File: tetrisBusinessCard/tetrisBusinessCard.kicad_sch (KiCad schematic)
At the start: 498 parts, among them J1 USB_B_Micro, SW1 SW_Push, SW2 SW_Push, SW3 SW_Push, SW4 SW_Push, SW5 SW_Push, SW6 SW_Push, SW7 SW_DPST_x2, SW8 SW_Push, U1 SC091413, U2 W25Q16JVUXIQ, U3 NCP1117-3.3_SOT223, Y1 ABMB-272-T3

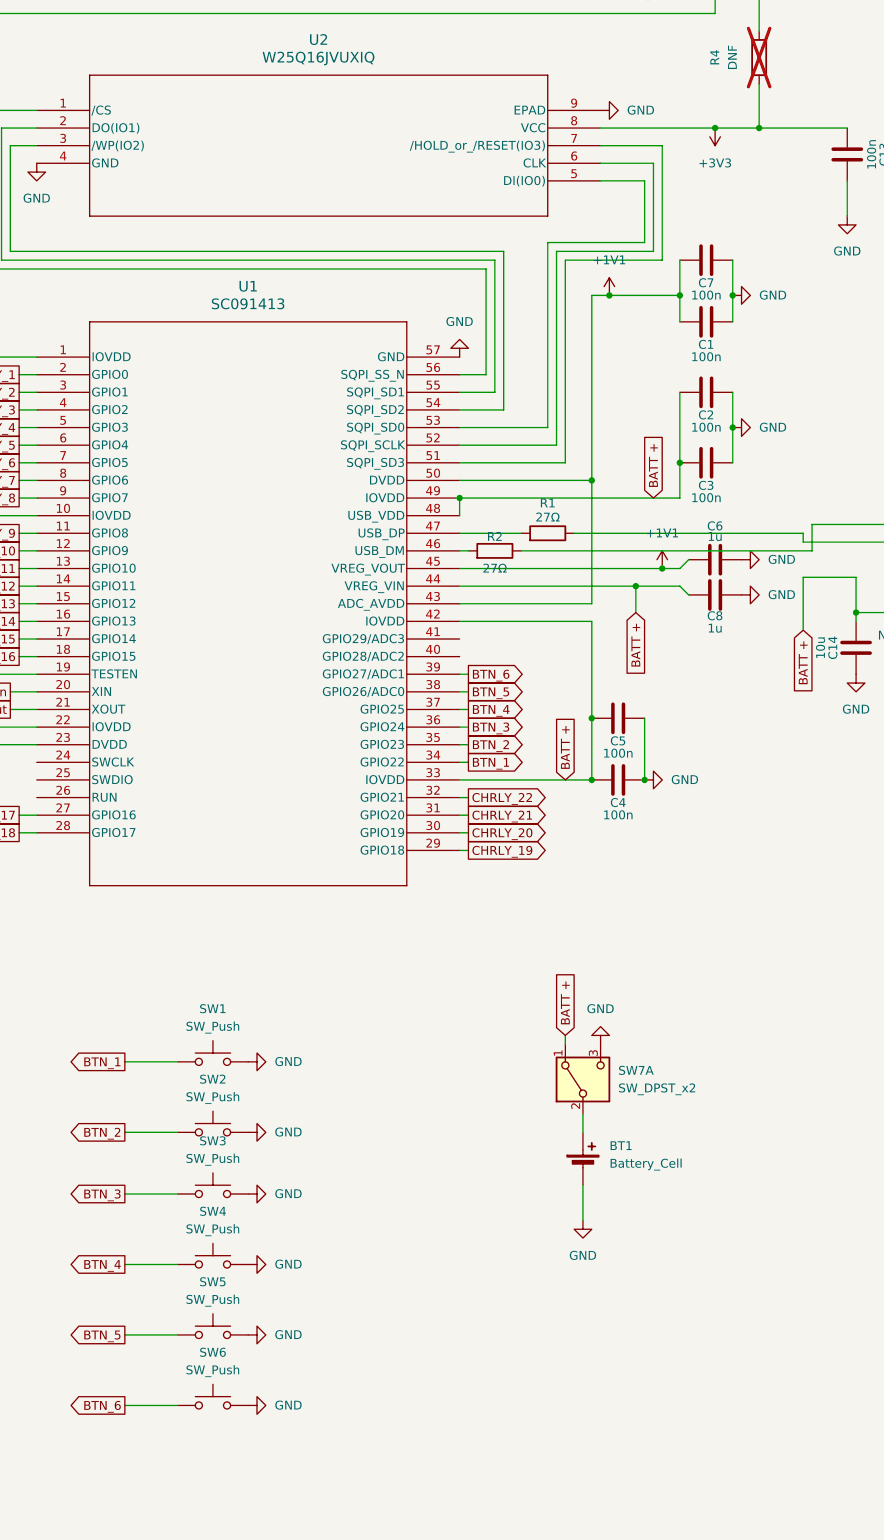
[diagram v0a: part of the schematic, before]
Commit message: Add capacitive touch symbol and update PCB partially
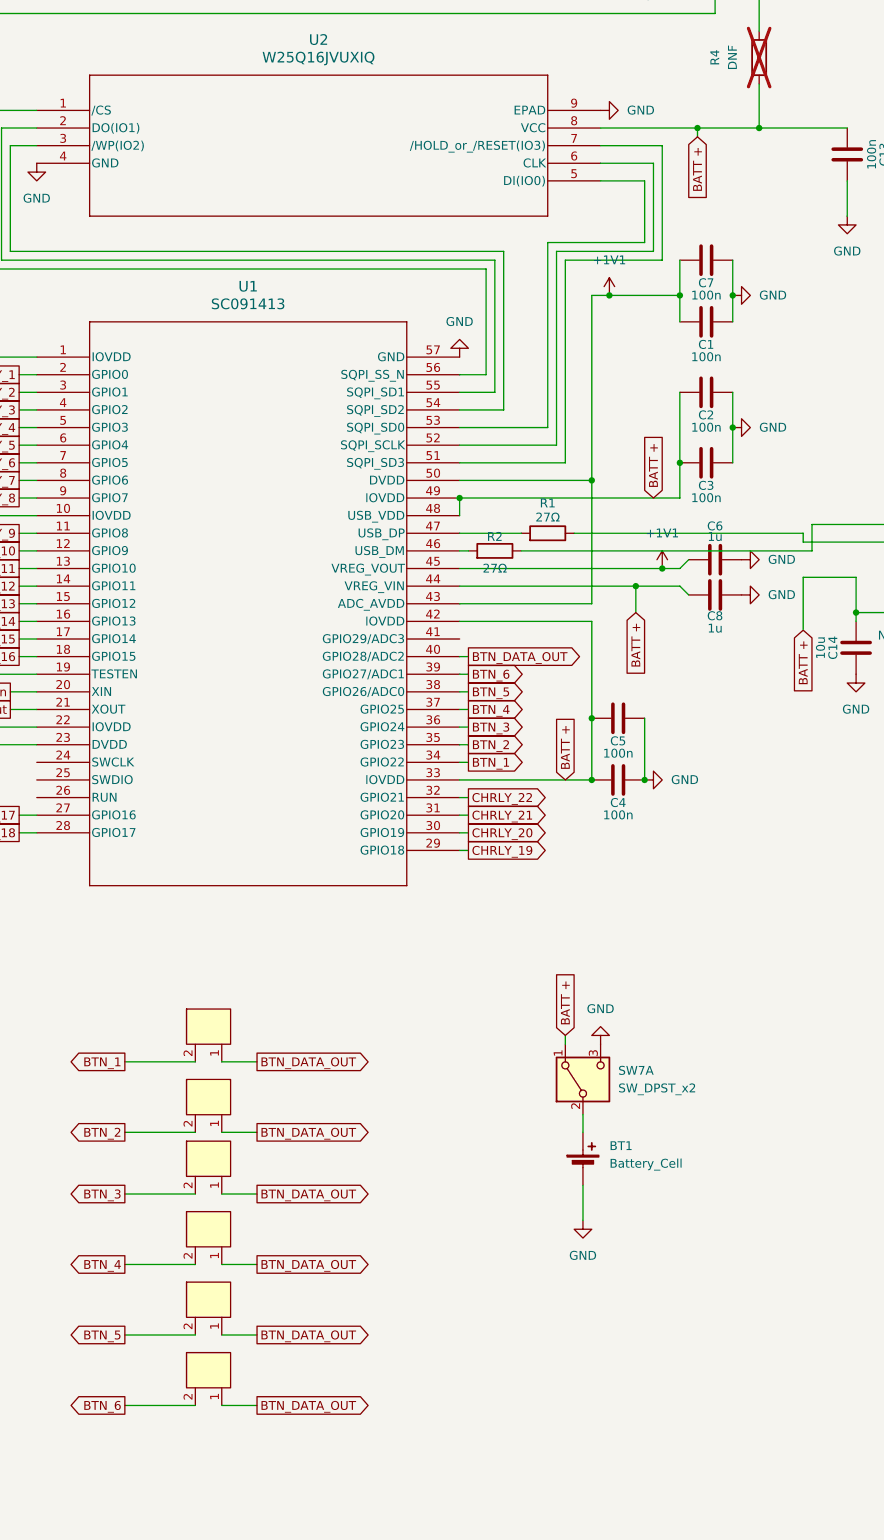
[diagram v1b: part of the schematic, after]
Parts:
- removed SW1, SW2, SW3, SW4, SW5, SW6: SW_Push, Button_Switch_SMD:SW_SPST_B3U-1000P, symbol Switch:SW_Push
- added U4, U5, U6, U7, U8, U9: ~, symbol MySymbols:CapacitiveTouch
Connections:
- net +3V3 is gone; now on net BATT +: C13.1, R4.1, U2.8 (VCC)
- net BTN_1: now also U4.2
- net BTN_2: now also U5.2
- net BTN_3: now also U6.2
- net BTN_4: now also U7.2
- net BTN_5: now also U8.2
- net BTN_6: now also U9.2
- net BTN_DATA_OUT: now reaches U1.40 (GPIO28/ADC2)
- net BTN_DATA_OUT: now also U4.1, U5.1, U6.1, U7.1, U8.1, U9.1

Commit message: pcb rev0.2
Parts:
- removed U4, U5, U6, U7, U8, U9: ~, symbol MySymbols:CapacitiveTouch
- added PogoConnector1: ~, MyFootprints:PogoConnector, symbol MySymbols:PogoConnector
- added R10, R11, R6, R7, R8, R9: 10kΩ, Resistor_SMD:R_0603_1608Metric, symbol Device:R
- added SW1, SW2, SW3, SW4, SW5, SW6: SW_Push, MyFootprints:SW_PTS647SM38SMTR2LFS_CNK, symbol Switch:SW_Push
- BT1, SW7: now not fitted
- C1, C10, C11, C12, C13, C14, C15, C16, C17, C2, C3, C4, C5, C6, C7, C8, C9: footprint Capacitor_SMD:C_0402_1005Metric -> Capacitor_SMD:C_0603_1608Metric
- D1, D10, D100, D101, D102, D103, D104, D105, D106, D107, D108, D109, D11, D110, D111, D112, D113, D114, D115, D116, D117, D118, D119, D12, D120, D121, D122, D123, D124, D125, D126, D127, D128, D129, D13, D130, D131, D132, D133, D134, D135, D136, D137, D138, D139, D14, D140, D141, D142, D143, D144, D145, D146, D147, D148, D149, D15, D150, D151, D152, D153, D154, D155, D156, D157, D158, D159, D16, D160, D161, D162, D163, D164, D165, D166, D167, D168, D169, D17, D170, D171, D172, D173, D174, D175, D176, D177, D178, D179, D18, D180, D181, D182, D183, D184, D185, D186, D187, D188, D189, D19, D190, D191, D192, D193, D194, D195, D196, D197, D198, D199, D2, D20, D200, D201, D202, D203, D204, D205, D206, D207, D208, D209, D21, D210, D211, D212, D213, D214, D215, D216, D217, D218, D219, D22, D220, D221, D222, D223, D224, D225, D226, D227, D228, D229, D23, D230, D231, D232, D233, D234, D235, D236, D237, D238, D239, D24, D240, D241, D242, D243, D244, D245, D246, D247, D248, D249, D25, D250, D251, D252, D253, D254, D255, D256, D257, D258, D259, D26, D260, D261, D262, D263, D264, D265, D266, D267, D268, D269, D27, D270, D271, D272, D273, D274, D275, D276, D277, D278, D279, D28, D280, D281, D282, D283, D284, D285, D286, D287, D288, D289, D29, D290, D291, D292, D293, D294, D295, D296, D297, D298, D299, D3, D30, D300, D301, D302, D303, D304, D305, D306, D307, D308, D309, D31, D310, D311, D312, D313, D314, D315, D316, D317, D318, D319, D32, D320, D321, D322, D323, D324, D325, D326, D327, D328, D329, D33, D330, D331, D332, D333, D334, D335, D336, D337, D338, D339, D34, D340, D341, D342, D343, D344, D345, D346, D347, D348, D349, D35, D350, D351, D352, D353, D354, D355, D356, D357, D358, D359, D36, D360, D361, D362, D363, D364, D365, D366, D367, D368, D369, D37, D370, D371, D372, D373, D374, D375, D376, D377, D378, D379, D38, D380, D381, D382, D383, D384, D385, D386, D387, D388, D389, D39, D390, D391, D392, D393, D394, D395, D396, D397, D398, D399, D4, D40, D400, D401, D402, D403, D404, D405, D406, D407, D408, D409, D41, D410, D411, D412, D413, D414, D415, D416, D417, D418, D419, D42, D420, D421, D422, D423, D424, D425, D426, D427, D428, D429, D43, D430, D431, D432, D433, D434, D435, D436, D437, D438, D439, D44, D440, D441, D442, D443, D444, D445, D446, D447, D448, D449, D45, D450, D451, D452, D453, D454, D455, D456, D457, D458, D459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: footprint LED_SMD:LED_0402_1005Metric -> MyFootprints:LED_0603_1608MetricAdjusted
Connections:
- net BTN_DATA_OUT is gone; now on net BTN_5: U1.40 (GPIO28/ADC2)
- net BATT +: now also PogoConnector1. (6), R10.1, R11.1, R6.1, R7.1, R8.1, R9.1
- net BTN_1: now also U1.36 (GPIO24), R10.2, SW1.1; no longer U1.34 (GPIO22)
- net BTN_2: now also U1.37 (GPIO25), R9.2, SW2.1; no longer U1.35 (GPIO23)
- net BTN_3: now also U1.38 (GPIO26/ADC0), R8.2, SW3.1; no longer U1.36 (GPIO24)
- net BTN_4: now also U1.39 (GPIO27/ADC1), R7.2, SW4.1; no longer U1.37 (GPIO25)
- net BTN_5: now also R6.2, SW5.1; no longer U1.38 (GPIO26/ADC0)
- net BTN_6: now also U1.41 (GPIO29/ADC3), R11.2, SW6.1; no longer U1.39 (GPIO27/ADC1)
- net CHRLY_1: now also U1.4 (GPIO2); no longer U1.2 (GPIO0)
- net CHRLY_10: now also U1.14 (GPIO11); no longer U1.12 (GPIO9)
- net CHRLY_11: now also U1.15 (GPIO12); no longer U1.13 (GPIO10)
- net CHRLY_12: now also U1.16 (GPIO13); no longer U1.14 (GPIO11)
- net CHRLY_13: now also U1.17 (GPIO14); no longer U1.15 (GPIO12)
- net CHRLY_14: now also U1.18 (GPIO15); no longer U1.16 (GPIO13)
- net CHRLY_15: now also U1.27 (GPIO16); no longer U1.17 (GPIO14)
- net CHRLY_16: now also U1.28 (GPIO17); no longer U1.18 (GPIO15)
- net CHRLY_17: now also U1.29 (GPIO18); no longer U1.27 (GPIO16)
- net CHRLY_18: now also U1.30 (GPIO19); no longer U1.28 (GPIO17)
- net CHRLY_19: now also U1.31 (GPIO20); no longer U1.29 (GPIO18)
- net CHRLY_2: now also U1.5 (GPIO3); no longer U1.3 (GPIO1)
- net CHRLY_20: now also U1.32 (GPIO21); no longer U1.30 (GPIO19)
- net CHRLY_21: now also U1.34 (GPIO22); no longer U1.31 (GPIO20)
- net CHRLY_22: now also U1.35 (GPIO23); no longer U1.32 (GPIO21)
- net CHRLY_3: now also U1.6 (GPIO4); no longer U1.4 (GPIO2)
- net CHRLY_4: now also U1.7 (GPIO5); no longer U1.5 (GPIO3)
- net CHRLY_5: now also U1.8 (GPIO6); no longer U1.6 (GPIO4)
- net CHRLY_6: now also U1.9 (GPIO7); no longer U1.7 (GPIO5)
- net CHRLY_7: now also U1.11 (GPIO8); no longer U1.8 (GPIO6)
- net CHRLY_8: now also U1.12 (GPIO9); no longer U1.9 (GPIO7)
- net CHRLY_9: now also U1.13 (GPIO10); no longer U1.11 (GPIO8)
- net GND: now also PogoConnector1. (6), SW1.2, SW2.2, SW3.2, SW4.2, SW5.2, SW6.2
- net SWCLK: now reaches U1.24 (SWCLK)
- net SWCLK: now also PogoConnector1. (6)
- net SWDIO: now reaches U1.25 (SWDIO)
- net SWDIO: now also PogoConnector1. (6)
- net D+: now reaches J1.3 (D+), R1.1
- net D-: now reaches J1.2 (D-), R2.1
- new net RX: PogoConnector1. (6), U1.3 (GPIO1)
- new net TX: PogoConnector1. (6), U1.2 (GPIO0)

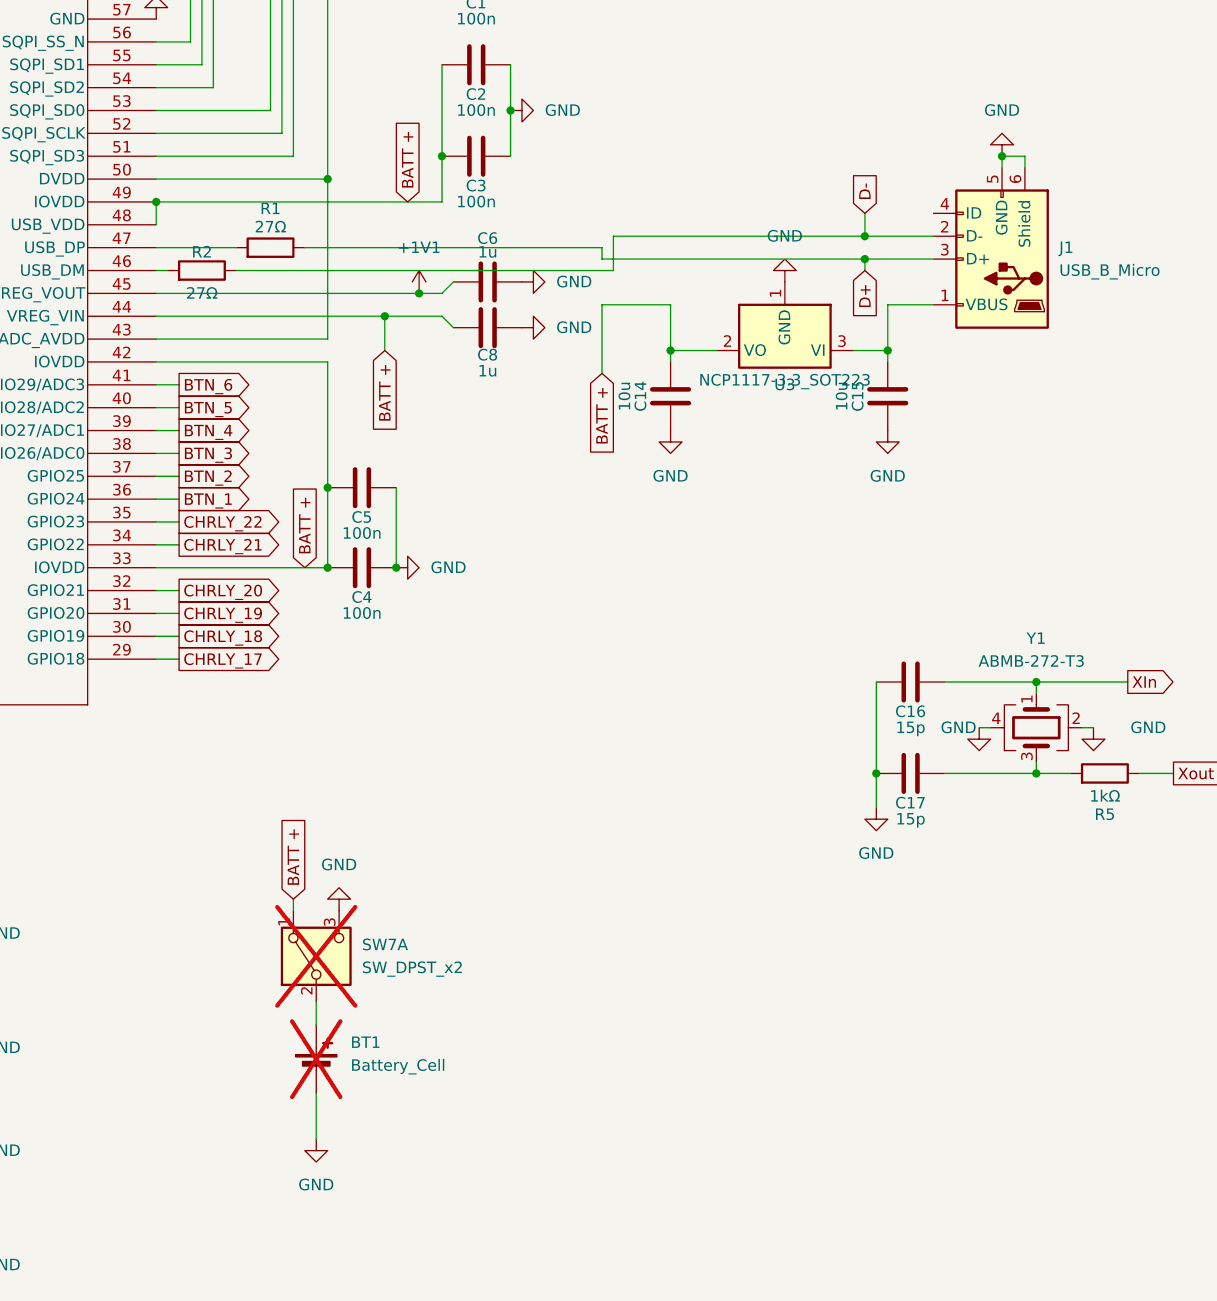
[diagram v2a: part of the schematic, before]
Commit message: RP2040 draws too much power. last commit before switching to stm32 based chips
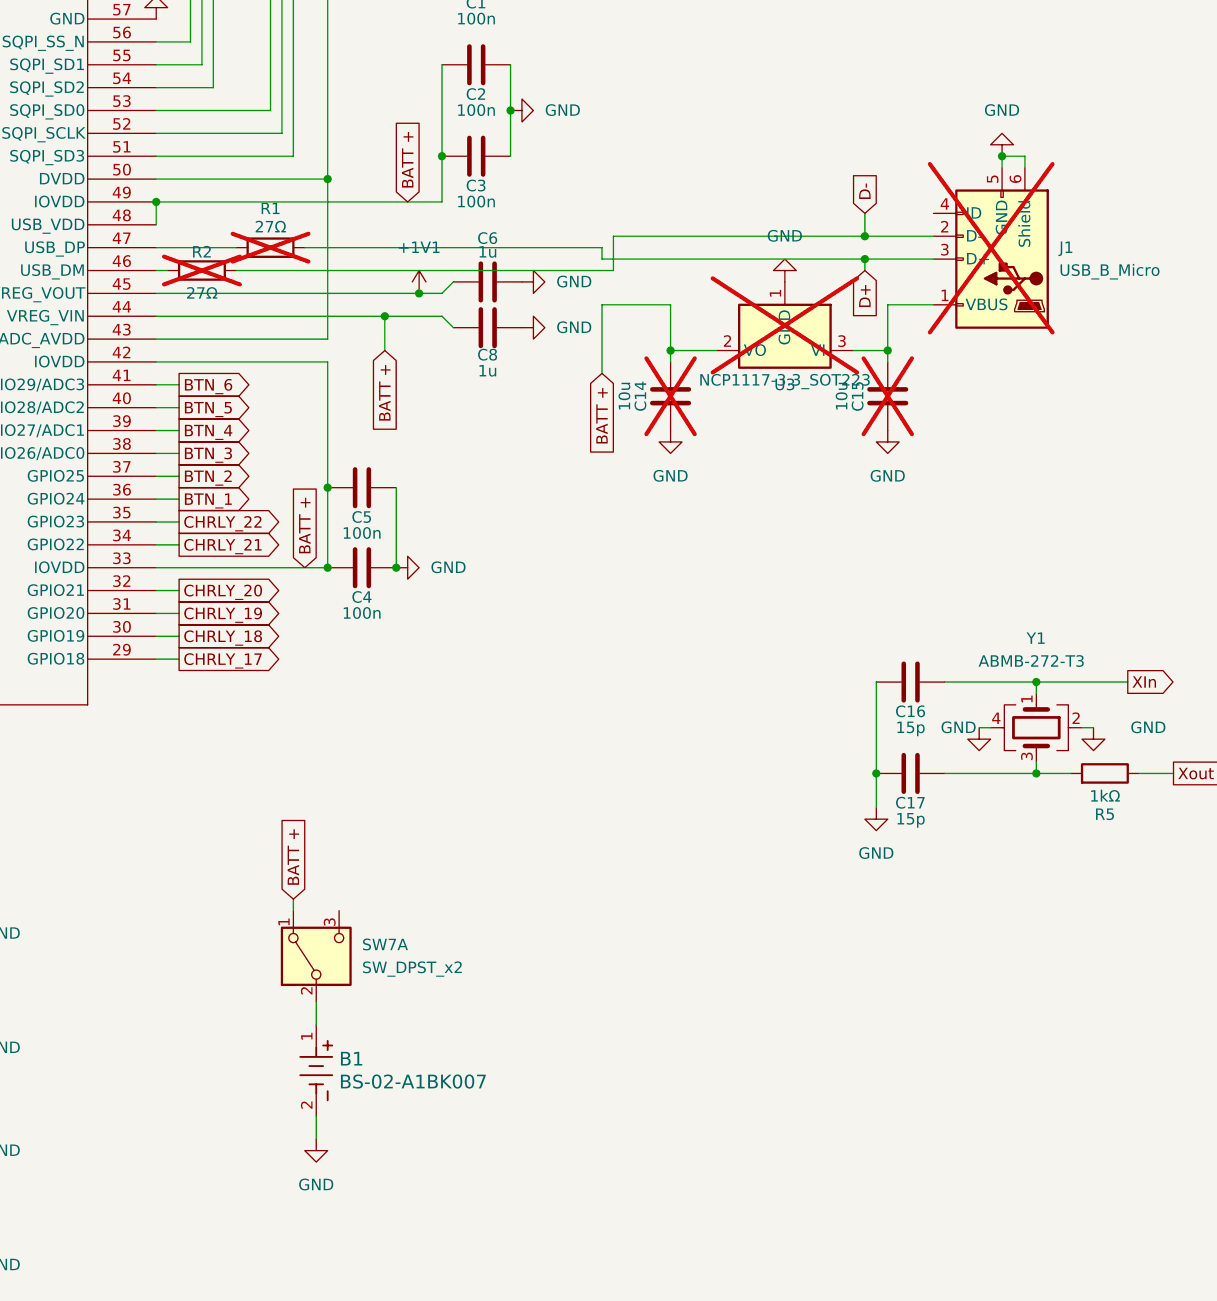
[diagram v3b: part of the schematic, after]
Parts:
- removed BT1: Battery_Cell, Battery:Battery_Panasonic_CR2032-HFN_Horizontal_CircularHoles, symbol Device:Battery_Cell
- added B1: BS-02-A1BK007, MyFootprints:BAT_BS-02_MYG, symbol MySymbols:BS-02-A1BK007
- C14, C15, J1, R1, R2, U3: now not fitted
- SW7: now fitted
- SW8: footprint Button_Switch_SMD:SW_SPST_B3U-1000P -> MyFootprints:SW_PTS647SM38SMTR2LFS_CNK
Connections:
- net GND: now also B1.2; no longer SW7.3 (C)
- net at SW7.2 (B): now also B1.1
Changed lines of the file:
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@@
 	(wire
 		(pts
+			(xy 575.31 250.19) (xy 575.31 247.65)
+		)
+		(stroke
+			(width 0)
+			(type default)
+		)
+	)
+	(wire
+		(pts
 			(xy 989.33 227.33) (xy 989.33 238.76)
 		)
@@
 	(wire
 		(pts
-			(xy 575.31 245.11) (xy 575.31 250.19)
-		)
-		(stroke
-			(width 0)
-			(type default)
-		)
-	)
-	(wire
-		(pts
 			(xy 999.49 101.6) (xy 1002.03 101.6)
 		)
@@
 	)
 	(symbol
-		(lib_id "power:GND")
-		(at 577.85 224.79 180)
-		(unit 1)
-		(exclude_from_sim no)
-		(in_bom yes)
-		(on_board yes)
-		(dnp no)
-		(fields_autoplaced yes)
-		(property "Reference" "#PWR028"
-			(at 577.85 218.44 0)
-			(effects
-				(font
-					(size 1.27 1.27)
-				)
-				(hide yes)
-			)
-		)
-		(property "Value" "GND"
-			(at 577.85 219.71 0)
-			(effects
-				(font
-					(size 1.27 1.27)
-				)
-			)
-		)
-		(property "Footprint" ""
-			(at 577.85 224.79 0)
-			(effects
-				(font
-					(size 1.27 1.27)
-				)
-				(hide yes)
-			)
-		)
-		(property "Datasheet" ""
-			(at 577.85 224.79 0)
-			(effects
-				(font
-					(size 1.27 1.27)
-				)
-				(hide yes)
-			)
-		)
-		(property "Description" "Power symbol creates a global label with name \"GND\" , ground"
-			(at 577.85 224.79 0)
-			(effects
-				(font
-					(size 1.27 1.27)
-				)
-				(hide yes)
-			)
-		)
-		(pin "1"
-		)
-		(instances
-			(project "tetrisBusinessCard"
-				(path "/81723559-87f8-4451-b8c4-8c04cfdf45bf"
-					(reference "#PWR028")
-					(unit 1)
-				)
-			)
-		)
-	)
-	(symbol
 		(lib_id "Device:LED")
 		(at 1037.59 193.04 0)
@@
 		(in_bom yes)
 		(on_board yes)
-		(dnp no)
+		(dnp yes)
 		(property "Reference" "C15"
 			(at 635.508 167.64 90)
@@
 	)
 	(symbol
-		(lib_id "Device:Battery_Cell")
-		(at 575.31 242.57 0)
-		(unit 1)
-		(exclude_from_sim no)
-		(in_bom yes)
-		(on_board yes)
-		(dnp yes)
-		(fields_autoplaced yes)
-		(property "Reference" "BT1"
-			(at 579.12 239.4584 0)
-			(effects
-				(font
-					(size 1.27 1.27)
-				)
-				(justify left)
-			)
-		)
-		(property "Value" "Battery_Cell"
-			(at 579.12 241.9984 0)
-			(effects
-				(font
-					(size 1.27 1.27)
-				)
-				(justify left)
-			)
-		)
-		(property "Footprint" "Battery:Battery_Panasonic_CR2032-HFN_Horizontal_CircularHoles"
-			(at 575.31 241.046 90)
-			(effects
-				(font
-					(size 1.27 1.27)
-				)
-				(hide yes)
-			)
-		)
-		(property "Datasheet" "~"
-			(at 575.31 241.046 90)
-			(effects
-				(font
-					(size 1.27 1.27)
-				)
-				(hide yes)
-			)
-		)
-		(property "Description" "Single-cell battery"
-			(at 575.31 242.57 0)
-			(effects
-				(font
-					(size 1.27 1.27)
-				)
-				(hide yes)
-			)
-		)
-		(pin "2"
-		)
-		(pin "1"
-		)
-		(instances
-			(project "tetrisBusinessCard"
-				(path "/81723559-87f8-4451-b8c4-8c04cfdf45bf"
-					(reference "BT1")
-					(unit 1)
-				)
-			)
-		)
-	)
-	(symbol
 		(lib_id "Device:LED")
 		(at 995.68 101.6 0)
@@
 		(in_bom yes)
 		(on_board yes)
-		(dnp no)
+		(dnp yes)
 		(property "Reference" "R1"
 			(at 570.23 146.812 90)
@@
 			)
 		)
-		(property "Footprint" "Button_Switch_SMD:SW_SPST_B3U-1000P"
+		(property "Footprint" "MyFootprints:SW_PTS647SM38SMTR2LFS_CNK"
 			(at 571.5 62.23 0)
 			(effects
@@
 		(in_bom yes)
 		(on_board yes)
-		(dnp no)
+		(dnp yes)
 		(property "Reference" "R2"
 			(at 562.61 151.638 90)
@@
 		(in_bom yes)
 		(on_board yes)
-		(dnp yes)
+		(dnp no)
 		(fields_autoplaced yes)
 		(property "Reference" "SW7"
@@
 		(in_bom yes)
 		(on_board yes)
-		(dnp no)
+		(dnp yes)
 		(property "Reference" "C14"
 			(at 611.378 167.64 90)
@@
 		(in_bom yes)
 		(on_board yes)
-		(dnp no)
+		(dnp yes)
 		(fields_autoplaced yes)
 		(property "Reference" "J1"
@@
 	)
 	(symbol
+		(lib_id "MySymbols:BS-02-A1BK007")
+		(at 575.31 237.49 270)
+		(unit 1)
+		(exclude_from_sim no)
+		(in_bom yes)
+		(on_board yes)
+		(dnp no)
+		(fields_autoplaced yes)
+		(property "Reference" "B1"
+			(at 577.85 241.2999 90)
+			(effects
+				(font
+					(size 1.524 1.524)
+				)
+				(justify left)
+			)
+		)
+		(property "Value" "BS-02-A1BK007"
+			(at 577.85 243.8399 90)
+			(effects
+				(font
+					(size 1.524 1.524)
+				)
+				(justify left)
+			)
+		)
+		(property "Footprint" "MyFootprints:BAT_BS-02_MYG"
+			(at 578.866 231.902 0)
+			(effects
+				(font
+					(size 1.27 1.27)
+					(italic yes)
+				)
+				(hide yes)
+			)
+		)
+		(property "Datasheet" "BS-02-A1BK007"
+			(at 580.644 232.664 0)
+			(effects
+				(font
+					(size 1.27 1.27)
+					(italic yes)
+				)
+				(hide yes)
+			)
+		)
+		(property "Description" ""
+			(at 575.31 237.49 0)
+			(effects
+				(font
+					(size 1.27 1.27)
+				)
+				(hide yes)
+			)
+		)
+		(pin "1"
+		)
+		(pin "2"
+		)
+		(instances
+			(project ""
+				(path "/81723559-87f8-4451-b8c4-8c04cfdf45bf"
+					(reference "B1")
+					(unit 1)
+				)
+			)
+		)
+	)
+	(symbol
 		(lib_id "Device:LED")
 		(at 1023.62 273.05 0)
@@
 		(in_bom yes)
 		(on_board yes)
-		(dnp no)
+		(dnp yes)
 		(property "Reference" "U3"
 			(at 627.38 166.37 0)
